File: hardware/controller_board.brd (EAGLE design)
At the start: 86 x 65.5 mm, 250 parts, among them J1 FRSKY-GIMBAL-FRYSKY, J11 USB-MICROA-AMPHENOL-10118192-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, J2 FRSKY-GIMBAL-FRYSKY, J3 USB-MINIB-EDAC-690-005-299-043, J4 AVR_SPI_PRG_6NS, J8 FRSKY-GIMBAL-2X-SERVO, J9 FRSKY-GIMBAL-2X-SERVO, P1 TEST-POINT, P2 TEST-POINT, P3 TEST-POINT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

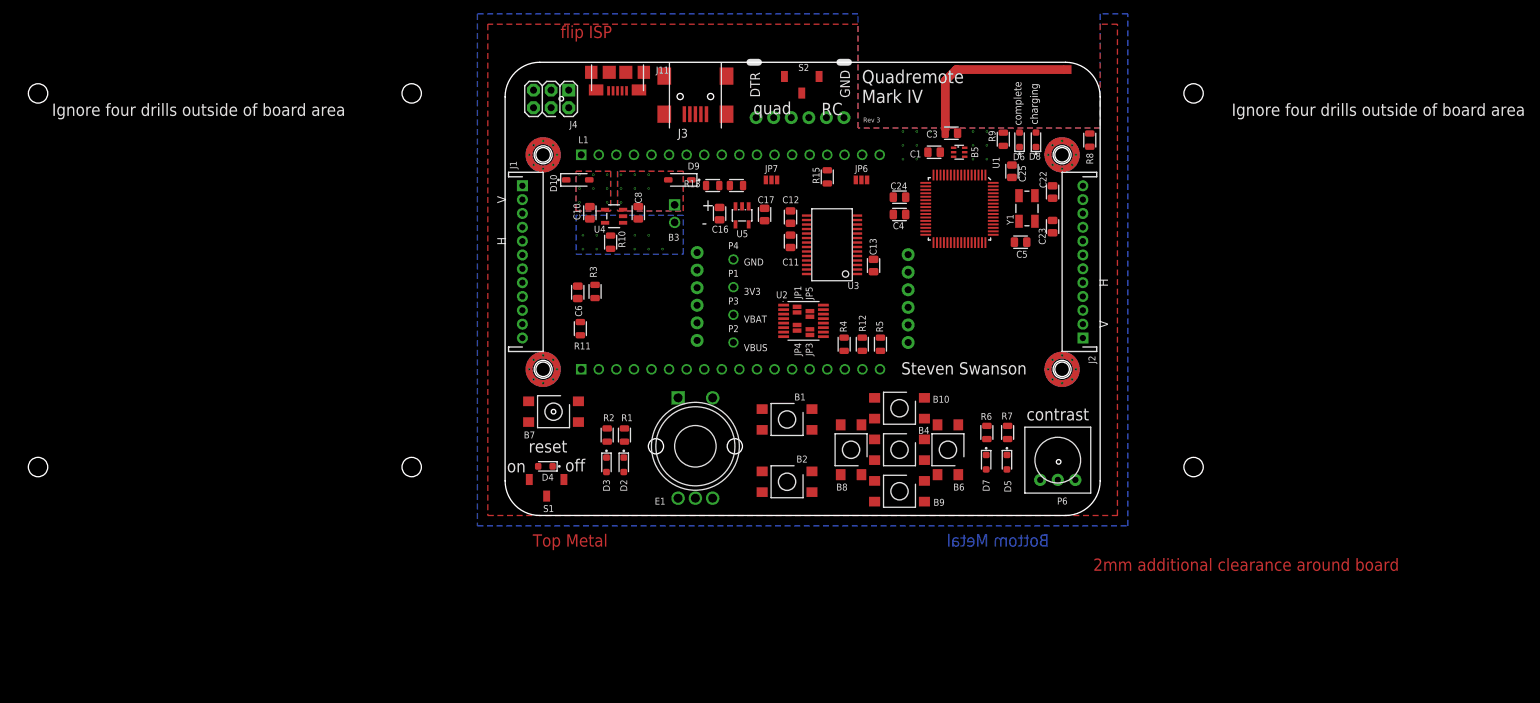
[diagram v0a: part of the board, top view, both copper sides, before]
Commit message: Remove option for 3v3 from FTDI.  Cleanup;  Edge-mounted switches.
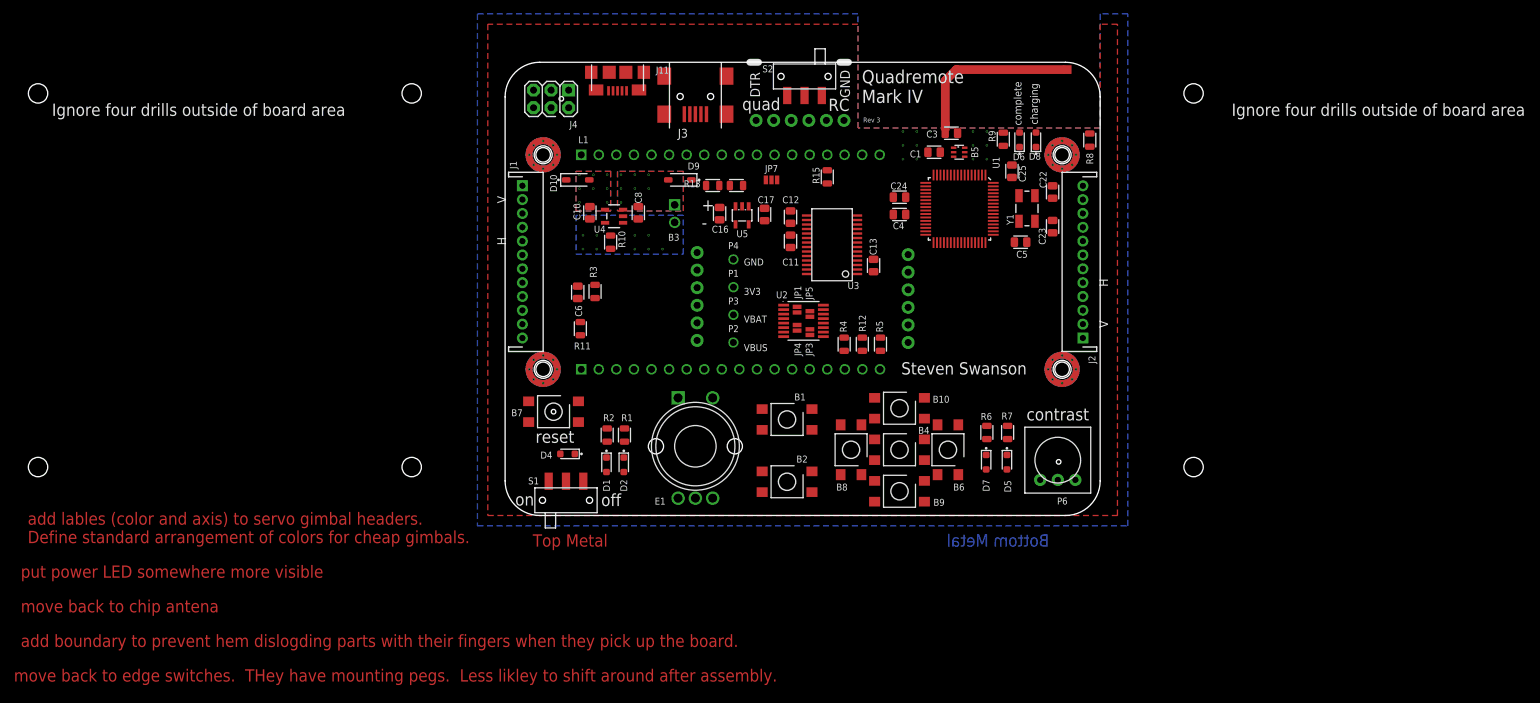
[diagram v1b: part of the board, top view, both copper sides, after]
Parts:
- removed JP6: JUMPER-SMT_3_1-NC_PASTE_NO-SILK, RemoteParts:SMT-JUMPER_3_1-NC_PASTE_NO-SILK
- S1, S2: value POWER-SWITCH-MFS201N-9-Z-SMD-VERTICAL -> POWER-SWITCH-MFS201N-9-ZJS102011SAQN; device RemoteParts:JS102011JCQN -> RemoteParts:JS102011SAQN
- moved D4 3.67 mm to (-34.7, -24.2)
- moved S1 3.33 mm to (-34.2, -31.8), turned to 0 degrees
- moved S2 1.26 mm to (0.28, 29.4)
- moved JP2 0.40 mm to (-0.38, 23.1)
- renumbered D3 to D1
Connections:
- removed net VREG3V3: C17.2, JP6.3, U5.5
- net 3V3: now also C17.2, S2.B, U5.5; no longer JP6.2, S2.3
- net FTDI3V3: no longer JP6.1
- net GND: now also S2.A; no longer S2.1
- net N$1: now also S1.C; no longer S1.2
- net PROG_SEL: now also S2.C; no longer S2.2
- net VBAT: now also S1.A; no longer S1.3
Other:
- board text added: "add boundary to prevent hem dislogding parts with their fingers when they pick up the board."
- board text added: "add lables (color and axis) to servo gimbal headers. Define standard arrangement of colors for cheap gimbals."
- board text added: "move back to chip antena"
- board text added: "move back to edge switches. THey have mounting pegs. Less likley to shift around after assembly."
- board text added: "put power LED somewhere more visible"
- board text removed: "2mm additional clearance around board"
- board text removed: "flip ISP"

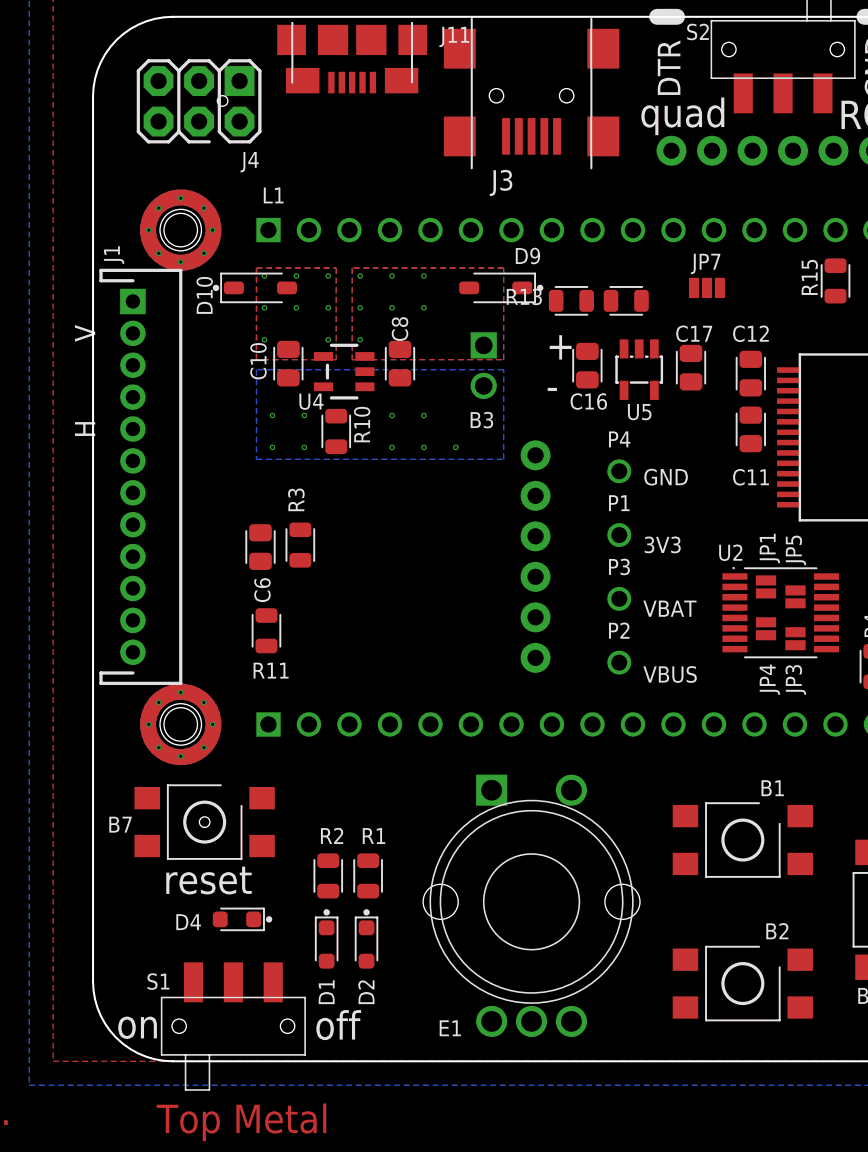
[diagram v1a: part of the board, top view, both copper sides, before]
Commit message: Bypass power switch.  Rearrange circuit to share input cap on vreg and bat charger
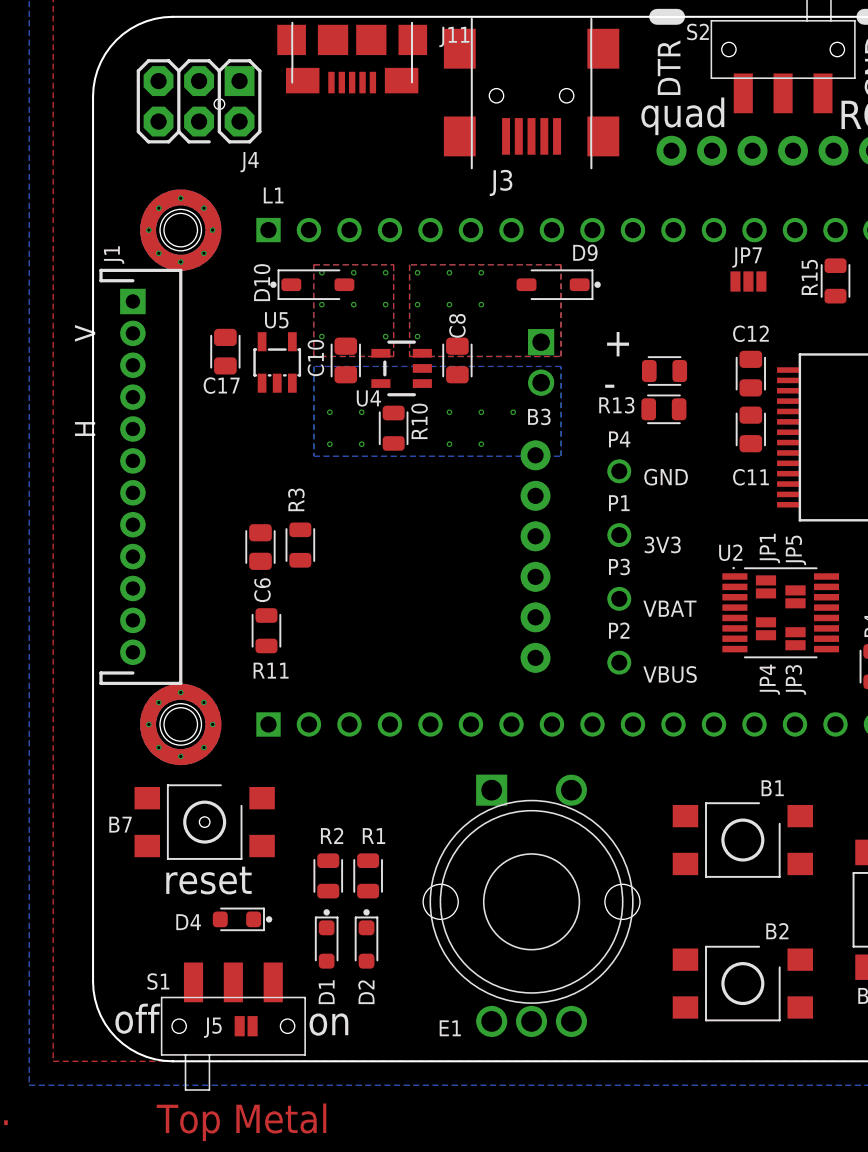
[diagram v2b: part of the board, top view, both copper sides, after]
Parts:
- removed C16: 1uF, quadparts_prebuilt:CAPC2012X140_HS
- added J5: JUMPER-SMT_2_NC_PASTE_NO-SILK, RemoteParts:SMT-JUMPER_2_NC_PASTE_NO-SILK
- moved C17 29.2 mm to (-34.7, 10.5), turned to 90 degrees
- moved U5 22.7 mm to (-31.4, 9.82), turned to 0 degrees
- moved R13 8.94 mm to (-7.20, 6.89)
- moved R14 5.01 mm to (-7.16, 9.29)
- moved V3 4.22 mm to (-16.6, 6.70)
- moved C10 3.61 mm to (-27.1, 9.95)
- moved C8 3.61 mm to (-20.1, 9.95)
- moved D10 3.61 mm to (-28.9, 14.7)
- moved R10 3.61 mm to (-24.1, 5.70)
- moved U4 3.61 mm to (-23.6, 9.45)
- moved V1 3.61 mm to (-28.6, 11.4)
- moved V19 3.61 mm to (-20.6, 4.70)
- moved V2 3.61 mm to (-28.6, 15.4)
- moved V23 3.61 mm to (-24.6, 11.4)
- moved V24 3.61 mm to (-24.6, 15.4)
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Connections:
- removed net N$1: D9.C, S1.C
- new net N$16: J5.2, S1.B, U5.3
- net GND: no longer C16.2
- net VBAT: now also D9.C, J5.1, S1.C; no longer C16.1, S1.A, U5.3

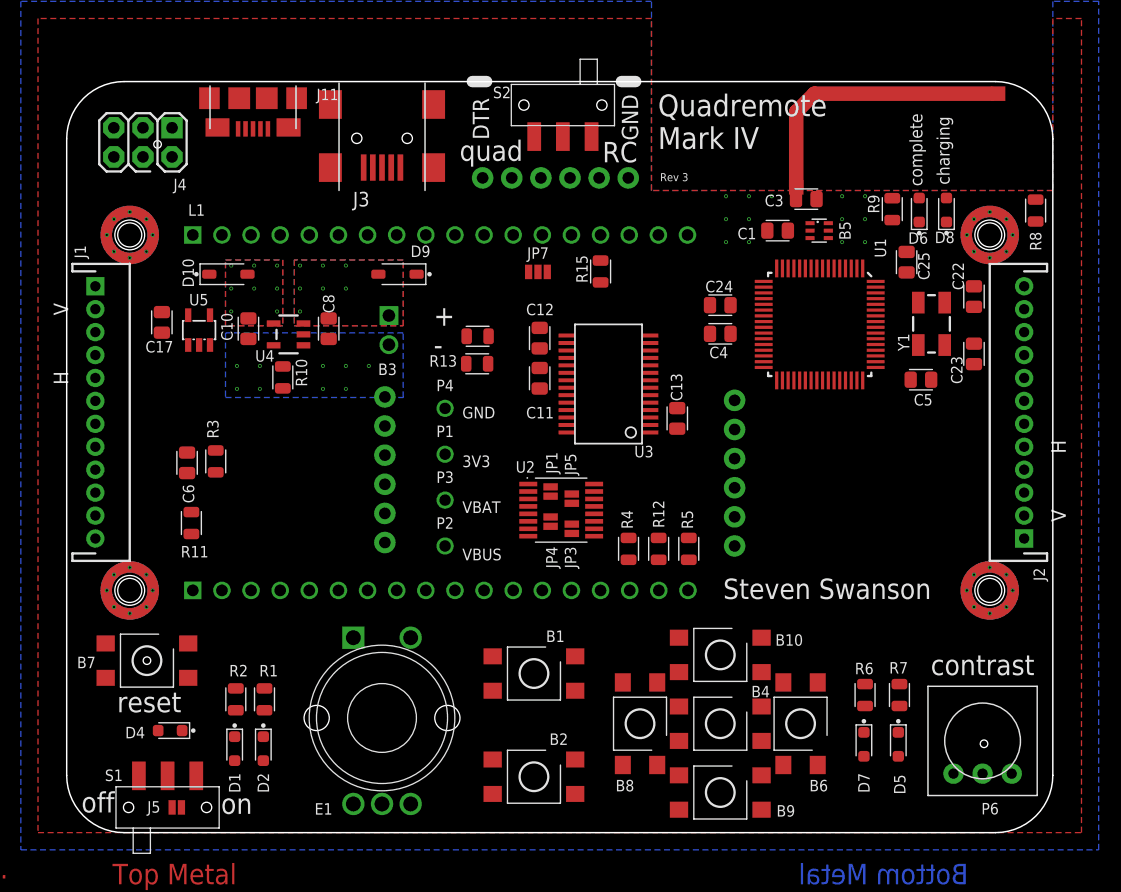
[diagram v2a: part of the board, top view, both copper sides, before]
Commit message: first steps toward silkscreen cleanup.  Shrunk everything and fixed typos
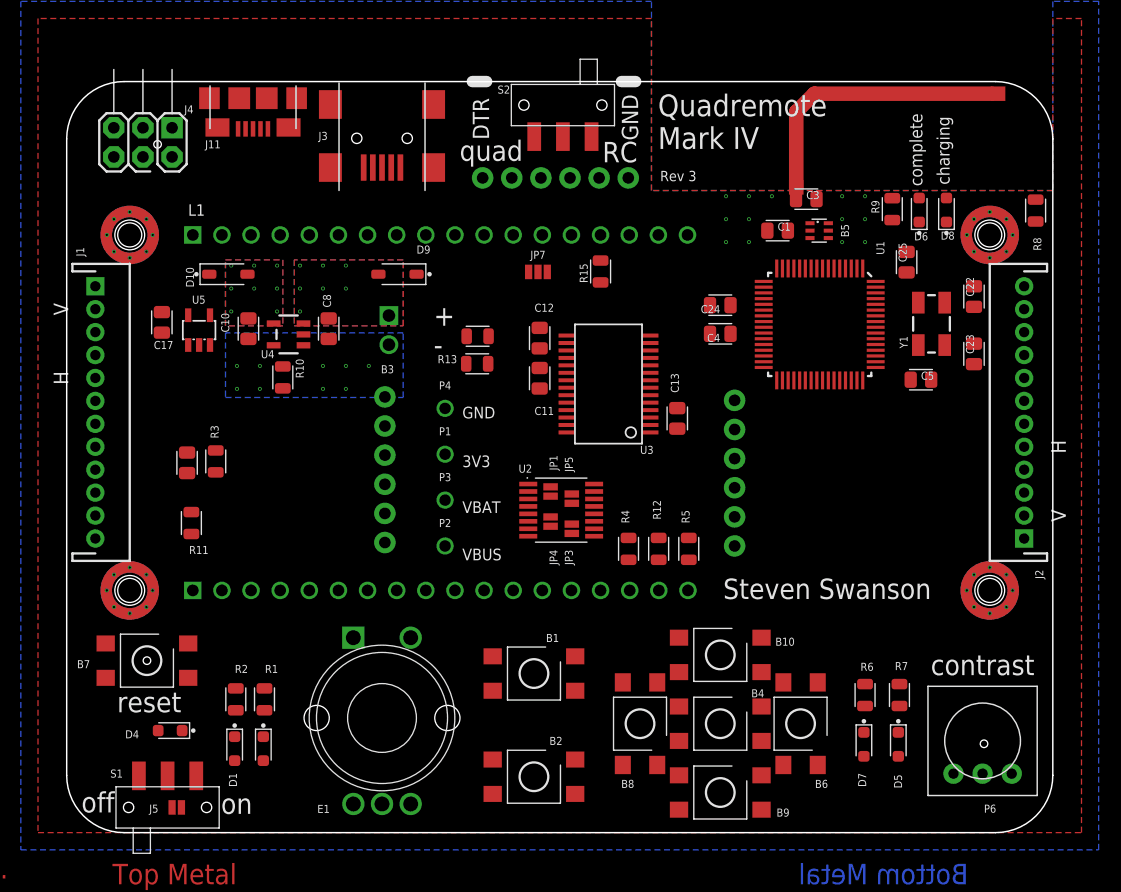
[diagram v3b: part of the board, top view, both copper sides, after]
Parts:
- D1, D4, D5, D6: value green -> Green
- D2, D7, D8: value RED -> Red

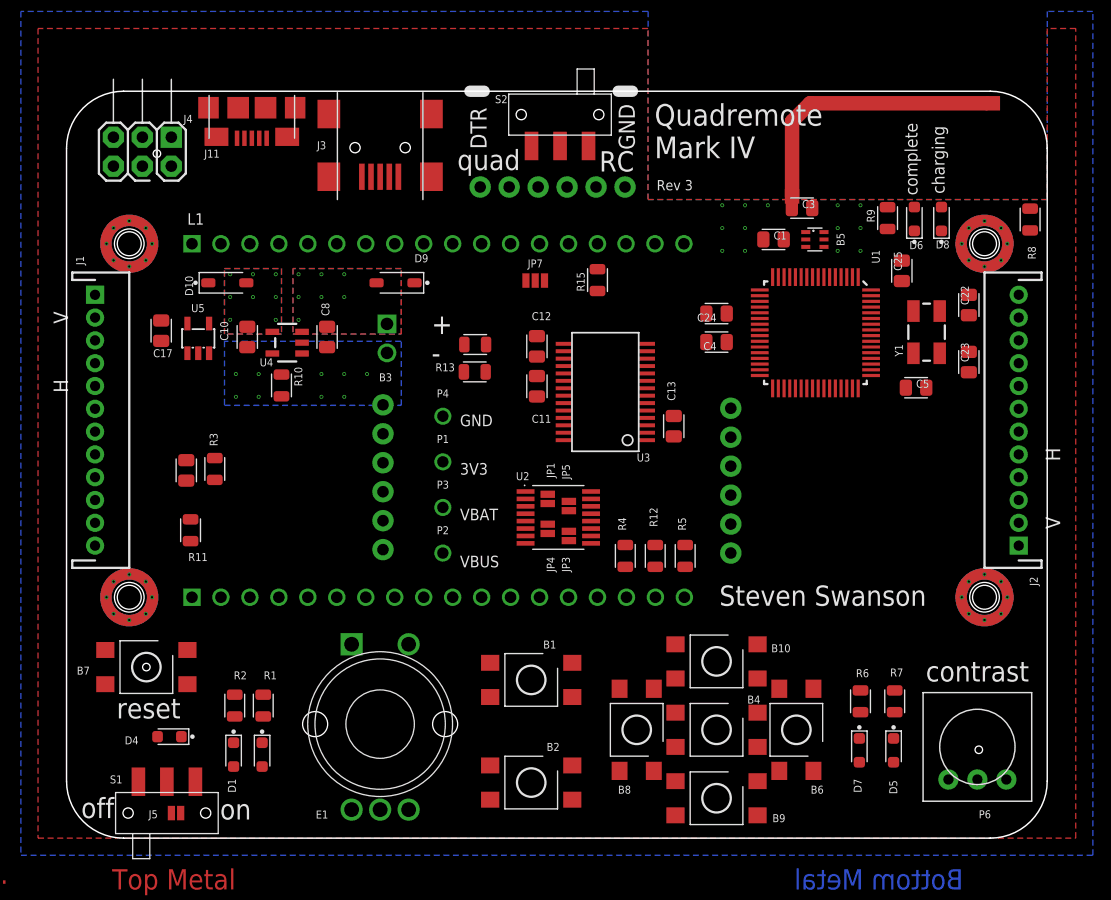
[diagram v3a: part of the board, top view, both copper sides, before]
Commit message: placed all reference designators and values
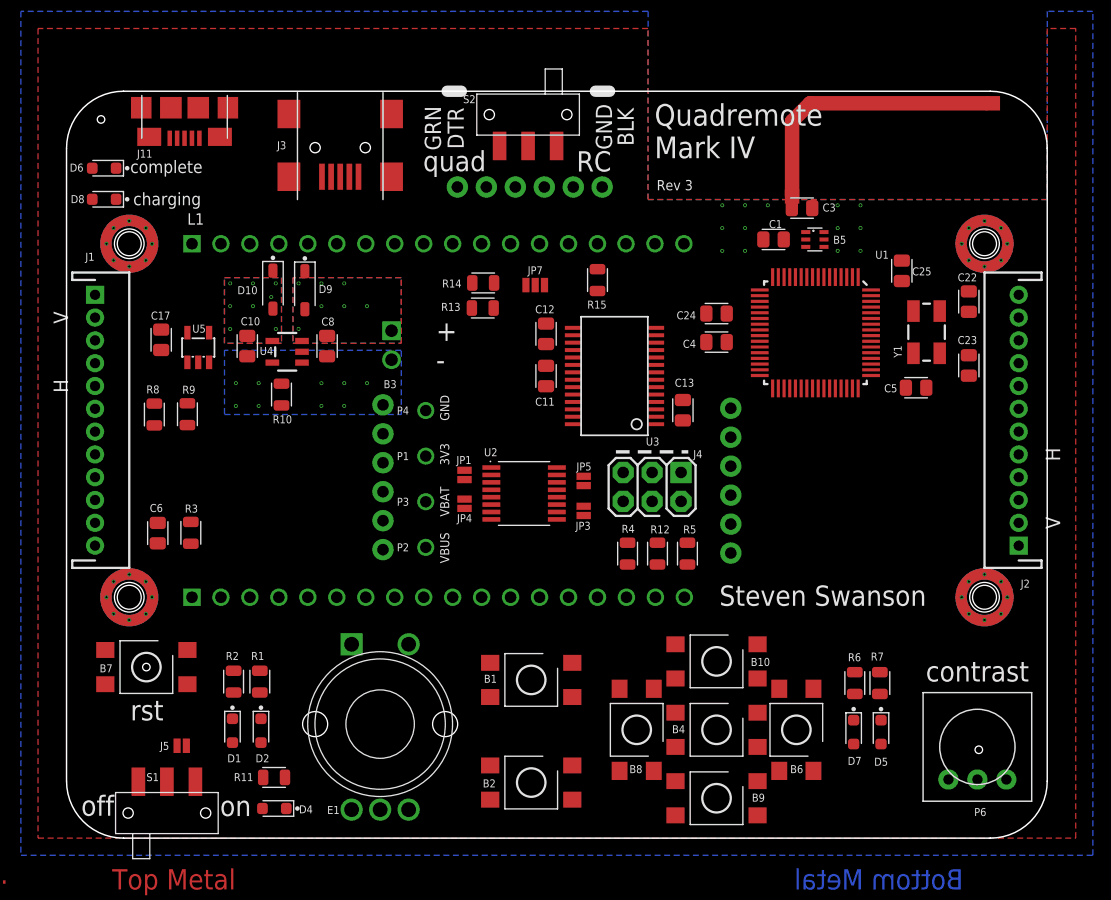
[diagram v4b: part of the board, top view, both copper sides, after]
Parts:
- moved R8 78.7 mm to (-35.3, 3.15)
- moved D8 75.0 mm to (-40.4, 22.9), turned to 0 degrees
- moved D6 72.8 mm to (-40.4, 25.6), turned to 0 degrees
- moved R9 63.8 mm to (-32.4, 3.17)
- moved J4 53.5 mm to (8.35, -3.20)
- moved R11 22.9 mm to (-24.8, -28.7), turned to 0 degrees
- moved D4 11.2 mm to (-25.5, -30.5)
- moved D9 7.98 mm to (-22.1, 14.1), turned to 270 degrees
- moved JP4 7.62 mm to (-8.10, -4.67)
- moved JP1 7.60 mm to (-8.10, -2.15)
- moved V32 6.05 mm to (-16.6, 12.7)
- moved C6 6.04 mm to (-35.0, -7.25)
- moved R3 5.98 mm to (-32.1, -7.22)
- moved J5 5.92 mm to (-32.9, -25.9)
- moved J11 5.90 mm to (-32.6, 27.4)
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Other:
- board text added: "BLK"
- board text added: "GRN"
- board text added: "rst"
- board text removed: "reset"
